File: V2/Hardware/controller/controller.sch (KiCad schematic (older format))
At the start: 45 parts, among them J0 Molex_PSU_F, J2 Flat_7seg_F, J3 Rpi_DATA_F_3.3V, Q0 BD139-16, Q1 BD139-16, Q2 BD139-16, Q3 BD139-16, Q4 BD139-16, Q5 BD139-16, Q6 BD139-16, U1 ATtiny2313-20PU

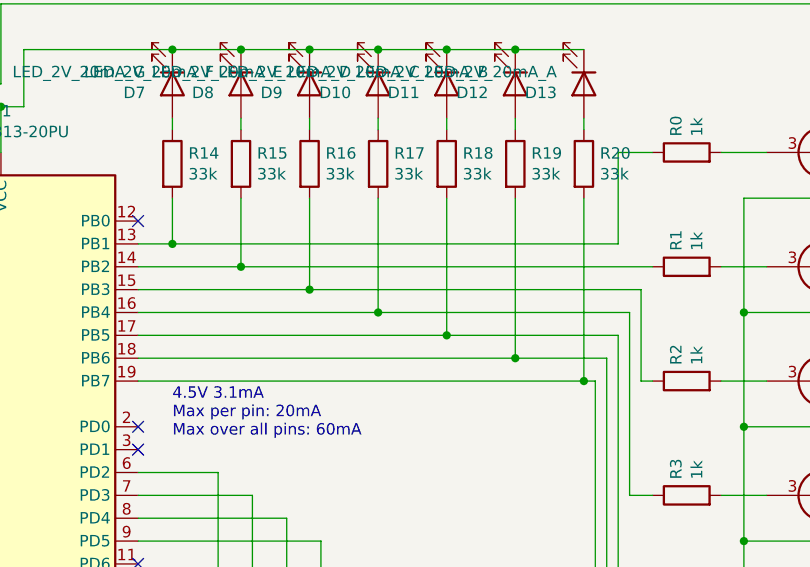
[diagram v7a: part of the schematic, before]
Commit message: Update resistor values
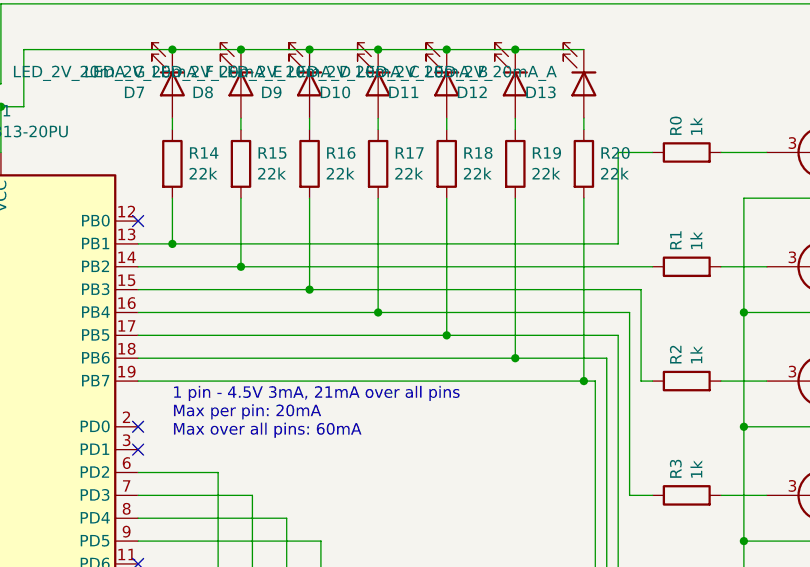
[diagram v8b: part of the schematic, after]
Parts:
- R14, R15, R16, R17, R18, R19, R20: value 33k -> 22k
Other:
- note added: "1 pin - 4.5V 3mA, 21mA over all pins \nMax per pin: 20mA\nMax over all pins: 60mA"
- note removed: "4.5V 3.1mA\nMax per pin: 20mA\nMax over all pins: 60mA"
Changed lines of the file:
@@
 P 5550 1600
 F 0 "R15" H 5620 1646 50  0000 L CNN
-F 1 "33k" H 5620 1555 50  0000 L CNN
+F 1 "22k" H 5620 1555 50  0000 L CNN
 F 2 "Resistor_THT:R_Axial_DIN0207_L6.3mm_D2.5mm_P15.24mm_Horizontal" V 5480 1600 50  0001 C CNN
 F 3 "~" H 5550 1600 50  0001 C CNN
@@
 P 5850 1600
 F 0 "R16" H 5920 1646 50  0000 L CNN
-F 1 "33k" H 5920 1555 50  0000 L CNN
+F 1 "22k" H 5920 1555 50  0000 L CNN
 F 2 "Resistor_THT:R_Axial_DIN0207_L6.3mm_D2.5mm_P15.24mm_Horizontal" V 5780 1600 50  0001 C CNN
 F 3 "~" H 5850 1600 50  0001 C CNN
@@
 P 6150 1600
 F 0 "R17" H 6220 1646 50  0000 L CNN
-F 1 "33k" H 6220 1555 50  0000 L CNN
+F 1 "22k" H 6220 1555 50  0000 L CNN
 F 2 "Resistor_THT:R_Axial_DIN0207_L6.3mm_D2.5mm_P15.24mm_Horizontal" V 6080 1600 50  0001 C CNN
 F 3 "~" H 6150 1600 50  0001 C CNN
@@
 P 6450 1600
 F 0 "R18" H 6520 1646 50  0000 L CNN
-F 1 "33k" H 6520 1555 50  0000 L CNN
+F 1 "22k" H 6520 1555 50  0000 L CNN
 F 2 "Resistor_THT:R_Axial_DIN0207_L6.3mm_D2.5mm_P10.16mm_Horizontal" V 6380 1600 50  0001 C CNN
 F 3 "~" H 6450 1600 50  0001 C CNN
@@
 P 6750 1600
 F 0 "R19" H 6820 1646 50  0000 L CNN
-F 1 "33k" H 6820 1555 50  0000 L CNN
+F 1 "22k" H 6820 1555 50  0000 L CNN
 F 2 "Resistor_THT:R_Axial_DIN0207_L6.3mm_D2.5mm_P10.16mm_Horizontal" V 6680 1600 50  0001 C CNN
 F 3 "~" H 6750 1600 50  0001 C CNN
@@
 P 7050 1600
 F 0 "R20" H 7120 1646 50  0000 L CNN
-F 1 "33k" H 7120 1555 50  0000 L CNN
+F 1 "22k" H 7120 1555 50  0000 L CNN
 F 2 "Resistor_THT:R_Axial_DIN0207_L6.3mm_D2.5mm_P10.16mm_Horizontal" V 6980 1600 50  0001 C CNN
 F 3 "~" H 7050 1600 50  0001 C CNN
@@
 12V cca 700mA
 Text Notes 5250 2800 0    50   ~ 0
-4.5V 3.1mA\nMax per pin: 20mA\nMax over all pins: 60mA
+1 pin - 4.5V 3mA, 21mA over all pins \nMax per pin: 20mA\nMax over all pins: 60mA
 Text Notes 2400 2650 0    50   ~ 0
 3.3V 800uA
@@
 P 5250 1600
 F 0 "R14" H 5320 1646 50  0000 L CNN
-F 1 "33k" H 5320 1555 50  0000 L CNN
+F 1 "22k" H 5320 1555 50  0000 L CNN
 F 2 "Resistor_THT:R_Axial_DIN0207_L6.3mm_D2.5mm_P10.16mm_Horizontal" V 5180 1600 50  0001 C CNN
 F 3 "~" H 5250 1600 50  0001 C CNN
